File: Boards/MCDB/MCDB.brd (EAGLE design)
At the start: 160 x 100 mm, 78 parts, among them IC1 MC33926, J1 USB_B_PTH, Y1 16MHz

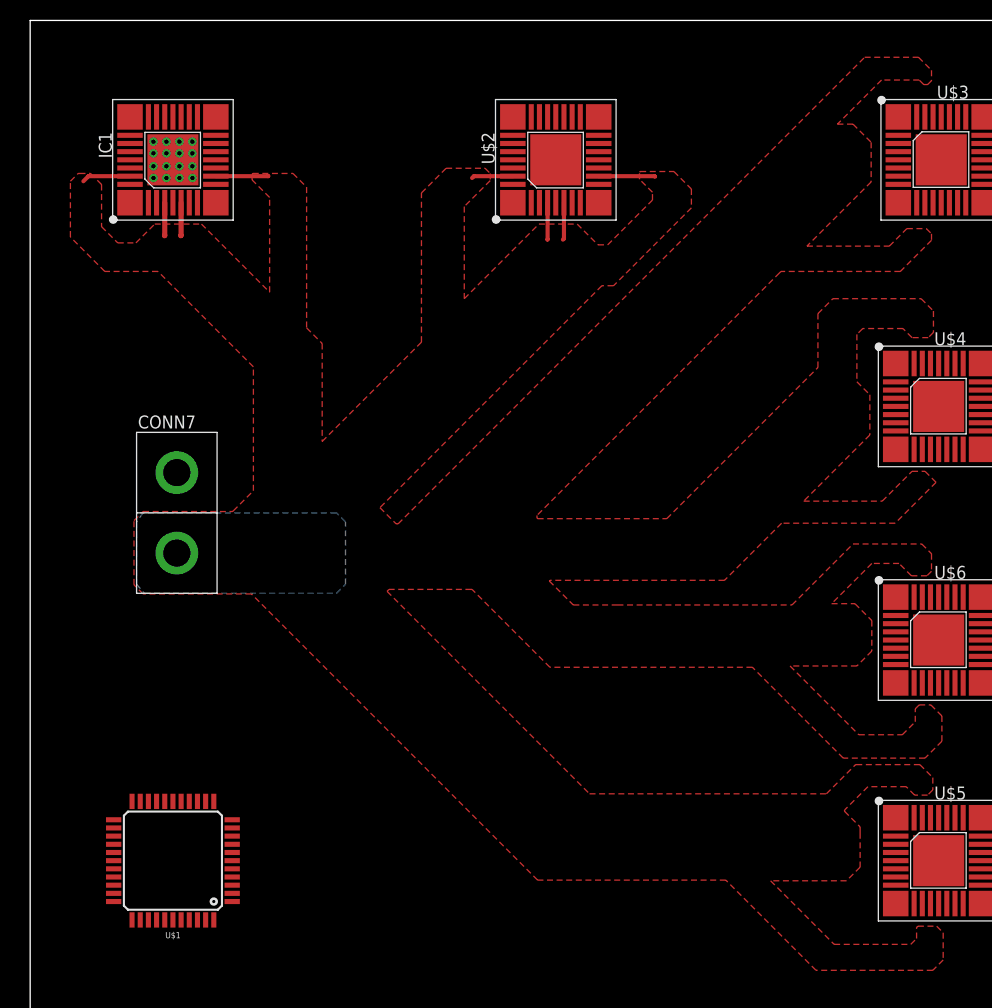
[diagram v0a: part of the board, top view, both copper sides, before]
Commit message: tried routing some signals from MCU
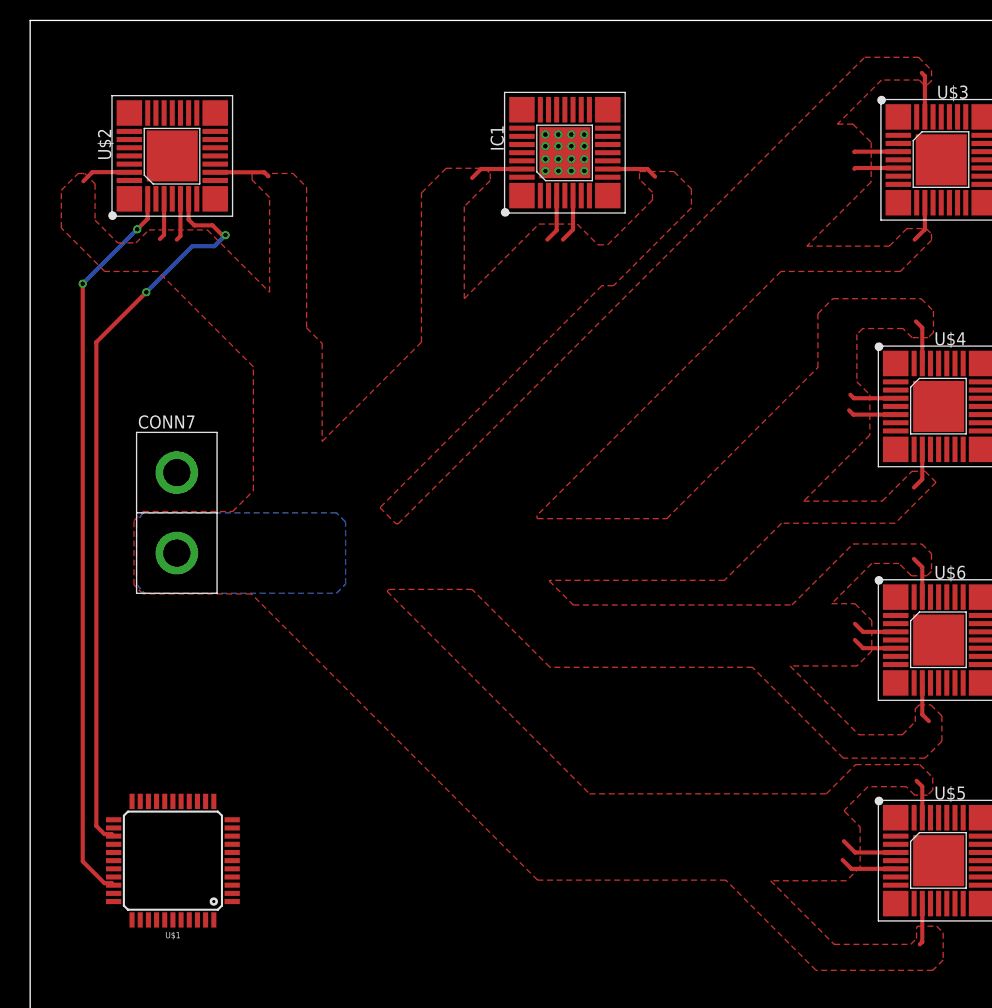
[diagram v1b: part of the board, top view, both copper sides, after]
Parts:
- moved IC1 38.4 mm to (52.3, 87.1)
- moved U$2 37.5 mm to (13.9, 86.7)
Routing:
- net VPWR: track 33.3 -> 108.2 mm
- net INV2: track 0.00 -> 72.8 mm, vias 0 -> 2
- net PWM2: track 0.00 -> 70.9 mm, vias 0 -> 2

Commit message: Continued work
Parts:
- removed U$2, U$3, U$4, U$5, U$6: MC33926, pie:PQFN-32
- added IC2, IC3, IC4, IC5, IC6: MC33926, pie:PQFN-32
- moved C21 181.5 mm to (100.8, 64.3), turned to 90 degrees
- moved CONN6 180.1 mm to (118.3, 57.1)
- moved C17 180.0 mm to (100.5, 34.5), turned to 90 degrees
- moved C24 176.0 mm to (101.3, 12.3), turned to 90 degrees
- moved CONN4 171.4 mm to (116.6, 85.2)
- moved CONN5 166.2 mm to (118.6, 25.8)
- moved C20 163.1 mm to (102.7, 43.4), turned to 90 degrees
- moved C9 161.9 mm to (100.4, 93.8), turned to 90 degrees
- moved CONN3 153.6 mm to (83.0, 116.3), turned to 90 degrees
- moved C16 153.2 mm to (101.7, 72.7), turned to 90 degrees
- moved C12 145.3 mm to (96.8, 101.7), turned to 180 degrees
- moved C5 131.1 mm to (74.9, 100.5), turned to 180 degrees
- moved CONN1 119.9 mm to (49.0, 115.0), turned to 90 degrees
- moved C13 109.9 mm to (40.7, 100.5), turned to 180 degrees
- moved ENCODER1 109.3 mm to (30.6, 114.5), turned to 180 degrees
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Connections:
- removed net CCP1: C5.1, U$3.32
- removed net N$1: C21.1, U$6.32
- removed net N$10: R6.4
- removed net N$14: R12.3
- removed net N$15: R12.4
- removed net N$2: R1.3
- removed net N$20: C9.1, U$4.32
- removed net N$3: R1.4
- removed net N$6: C5.2, C6.2, C8.PLUS
- removed net N$8: C17.1, U$5.32
- removed net N$9: R6.3
- new net CCP2: C1.1, IC2.32
- new net CCP4: C9.1, IC4.32
- new net CCP5: C17.1, IC5.32
- new net CCP6: C21.1, IC6.32
- net CCP: now also C13.1, IC1.32; no longer C1.1, U$2.32
- net CCP3: now also C5.1, IC3.32; no longer C13.1, IC1.32
- net FB2: now also IC2.8; no longer U$2.8
- net FB3: now also IC3.8; no longer U$3.8
- net FB4: now also IC4.8; no longer U$4.8
- net FB5: now also IC5.8; no longer U$5.8
- net FB6: now also IC6.8; no longer U$6.8
- net GND: now also IC2.18, IC2.19, IC2.20, IC2.22, IC2.23, IC2.24, IC2.26, IC2.3, IC2.5, IC2.MID, IC3.18, IC3.19, IC3.20, IC3.22, IC3.23, IC3.24, IC3.26, IC3.3, IC3.5, IC3.MID, IC4.18, IC4.19, IC4.20, IC4.22, IC4.23, IC4.24, IC4.26, IC4.3, IC4.5, IC4.MID, IC5.18, IC5.19, IC5.20, IC5.22, IC5.23, IC5.24, IC5.26, IC5.3, IC5.5, IC5.MID, IC6.18, IC6.19, IC6.20, IC6.22, IC6.23, IC6.24, IC6.26, IC6.3, IC6.5, IC6.MID; no longer U$2.18, U$2.19, U$2.20, U$2.22, U$2.23, U$2.24, U$2.26, U$2.3, U$2.5, U$2.MID, U$3.18, U$3.19, U$3.20, U$3.22, U$3.23, U$3.24, U$3.26, U$3.3, U$3.5, U$3.MID, U$4.18, U$4.19, U$4.20, U$4.22, U$4.23, U$4.24, U$4.26, U$4.3, U$4.5, U$4.MID, U$5.18, U$5.19, U$5.20, U$5.22, U$5.23, U$5.24, U$5.26, U$5.3, U$5.5, U$5.MID, U$6.18, U$6.19, U$6.20, U$6.22, U$6.23, U$6.24, U$6.26, U$6.3, U$6.5, U$6.MID
- net INV2: now also IC2.7; no longer U$2.7
- net INV3: now also IC3.7; no longer U$3.7
- net INV4: now also IC4.7; no longer U$4.7
- net INV5: now also IC5.7; no longer U$5.7
- net INV6: now also IC6.7; no longer U$6.7
- net OUT10: now also IC5.27, IC5.28, IC5.29, IC5.30; no longer U$5.27, U$5.28, U$5.29, U$5.30
- net OUT11: now also IC6.12, IC6.13, IC6.14, IC6.15; no longer U$6.12, U$6.13, U$6.14, U$6.15
- net OUT12: now also IC6.27, IC6.28, IC6.29, IC6.30; no longer U$6.27, U$6.28, U$6.29, U$6.30
- net OUT3: now also IC2.12, IC2.13, IC2.14, IC2.15; no longer U$2.12, U$2.13, U$2.14, U$2.15
- net OUT4: now also IC2.27, IC2.28, IC2.29, IC2.30; no longer U$2.27, U$2.28, U$2.29, U$2.30
- net OUT5: now also IC3.12, IC3.13, IC3.14, IC3.15; no longer U$3.12, U$3.13, U$3.14, U$3.15
- net OUT6: now also IC3.27, IC3.28, IC3.29, IC3.30; no longer U$3.27, U$3.28, U$3.29, U$3.30
- net OUT7: now also IC4.12, IC4.13, IC4.14, IC4.15; no longer U$4.12, U$4.13, U$4.14, U$4.15
- net OUT8: now also IC4.27, IC4.28, IC4.29, IC4.30; no longer U$4.27, U$4.28, U$4.29, U$4.30
- net OUT9: now also IC5.12, IC5.13, IC5.14, IC5.15; no longer U$5.12, U$5.13, U$5.14, U$5.15
- net PWM2: now also IC2.2; no longer U$2.2
- net PWM3: now also IC3.2; no longer U$3.2
- net PWM4: now also IC4.2; no longer U$4.2
- net PWM5: now also IC5.2; no longer U$5.2
- net PWM6: now also IC6.2; no longer U$6.2
- net VCC: now also IC2.1, IC2.10, IC2.16, IC3.1, IC3.10, IC3.16, IC4.1, IC4.10, IC4.16, IC5.1, IC5.10, IC5.16, IC6.1, IC6.10, IC6.16, R1.3, R1.4, R12.3, R12.4, R6.3, R6.4; no longer U$2.1, U$2.10, U$2.16, U$3.1, U$3.10, U$3.16, U$4.1, U$4.10, U$4.16, U$5.1, U$5.10, U$5.16, U$6.1, U$6.10, U$6.16
- net VPWR: now also C5.2, C6.2, C8.PLUS, IC2.11, IC2.31, IC2.4, IC2.6, IC3.11, IC3.31, IC3.4, IC3.6, IC4.11, IC4.31, IC4.4, IC4.6, IC5.11, IC5.31, IC5.4, IC5.6, IC6.11, IC6.31, IC6.4, IC6.6; no longer U$2.11, U$2.31, U$2.4, U$2.6, U$3.11, U$3.31, U$3.4, U$3.6, U$4.11, U$4.31, U$4.4, U$4.6, U$5.11, U$5.31, U$5.4, U$5.6, U$6.11, U$6.31, U$6.4, U$6.6
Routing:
- net VPWR: track 108.2 -> 33.4 mm
- net GND: track 0.00 -> 23.4 mm, vias 0 -> 3
- net OUT3: track 0.00 -> 17.7 mm
- net OUT4: track 0.00 -> 17.6 mm
- net VCC: track 0.00 -> 13.8 mm, vias 0 -> 2
- net INV2: track 72.8 -> 66.8 mm
- net CCP2: track 0.00 -> 3.73 mm
- net CCP5: track 0.00 -> 3.40 mm
- net CCP: track 0.00 -> 3.34 mm
- net CCP3: track 0.00 -> 3.27 mm
- net CCP4: track 0.00 -> 3.27 mm
- net CCP6: track 0.00 -> 3.15 mm
- net PWM2: track 70.9 -> 68.1 mm
- net OUT9: track 0.00 -> 2.40 mm
- net OUT6: track 0.00 -> 2.40 mm
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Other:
- board size 160 x 100 mm -> 160 x 127 mm
